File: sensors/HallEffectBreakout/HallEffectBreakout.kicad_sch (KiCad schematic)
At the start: 0 parts

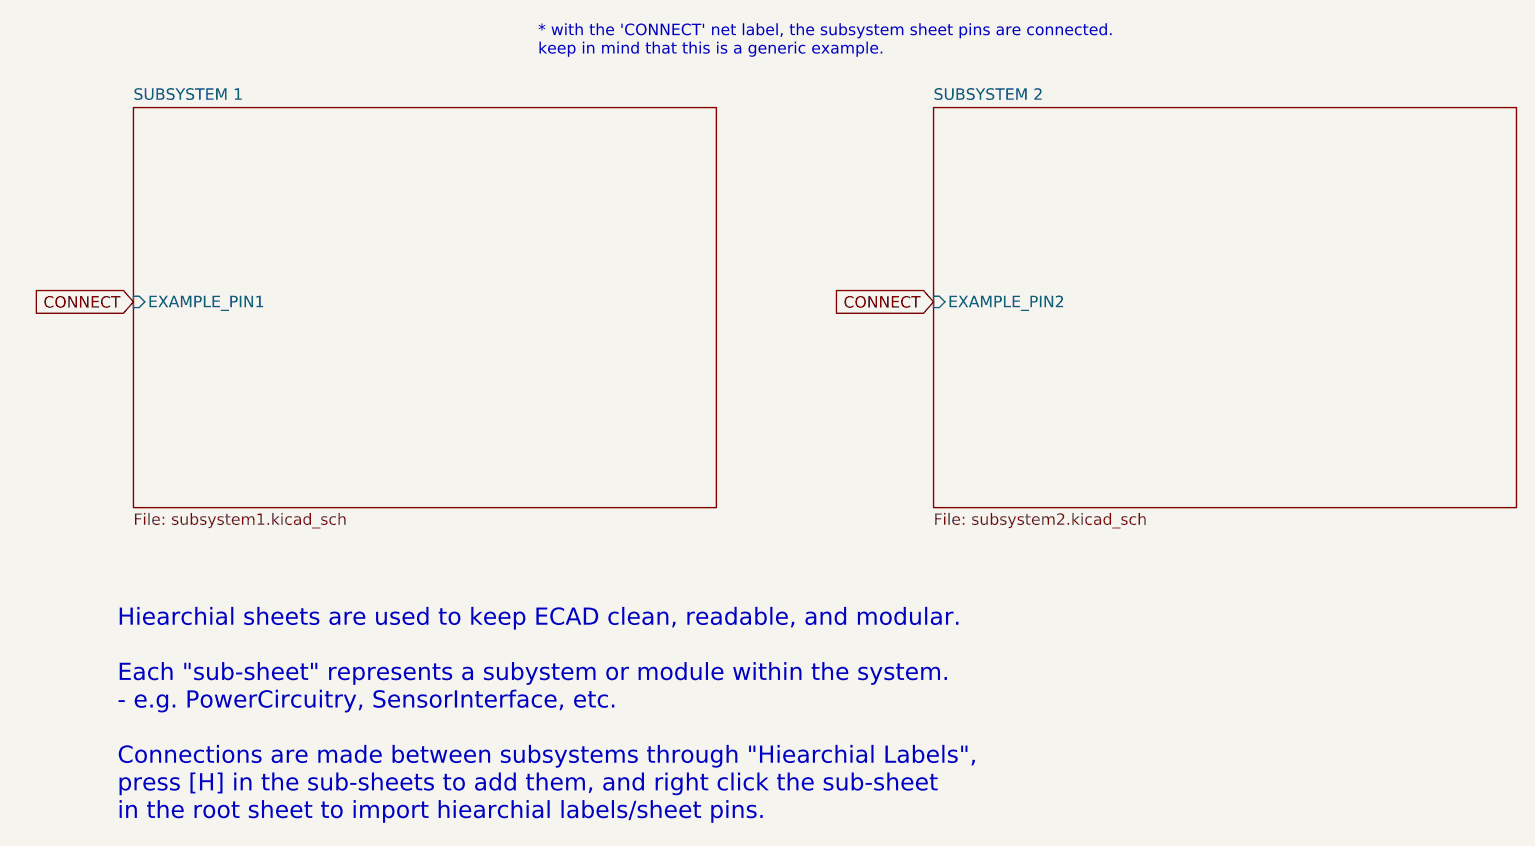
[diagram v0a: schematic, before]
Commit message: Removed Unused Template & Added TMAG5723
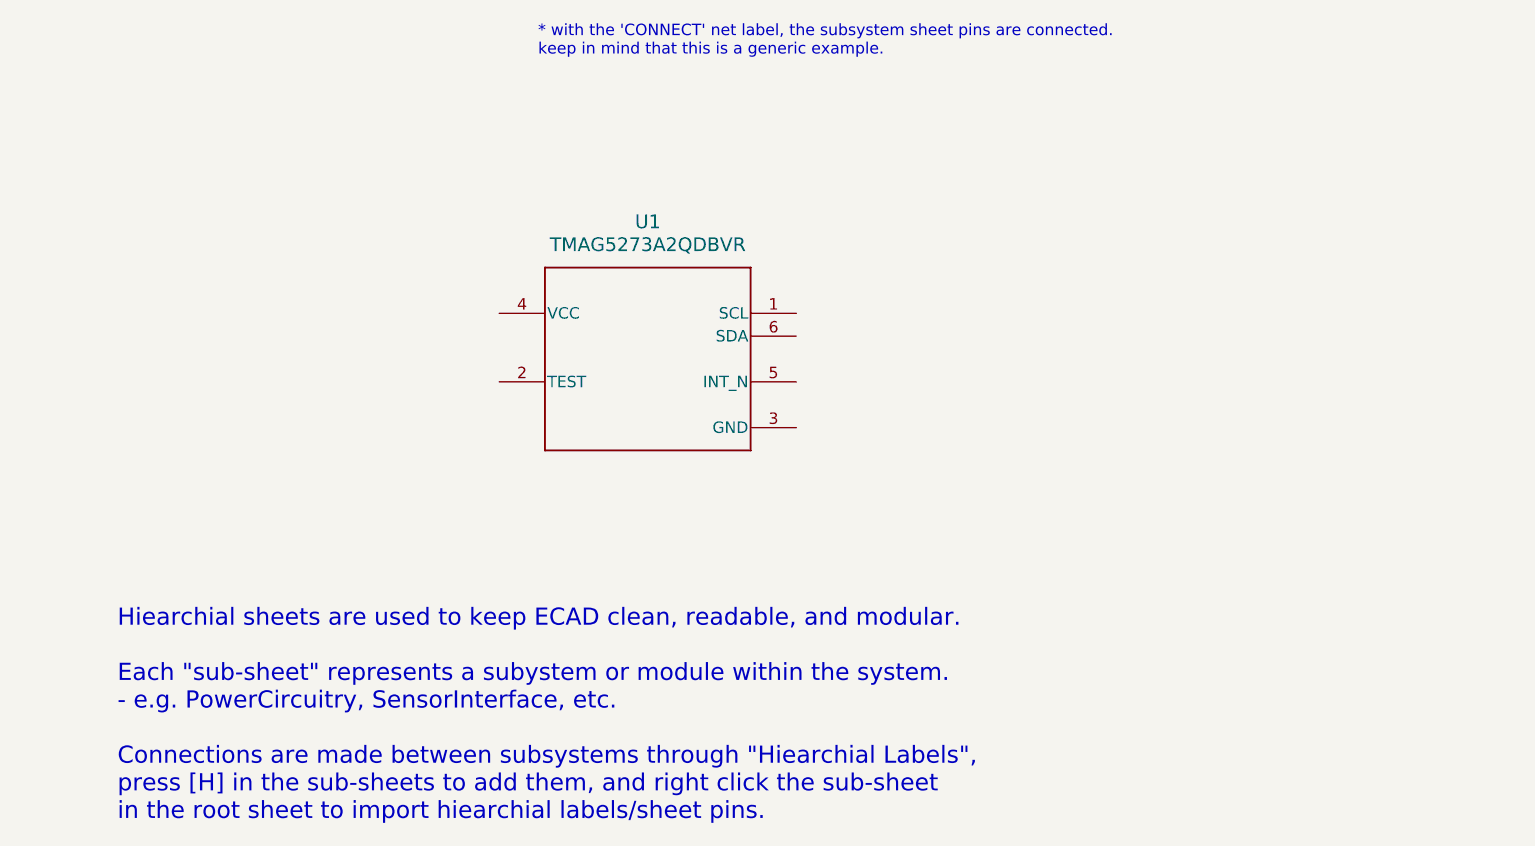
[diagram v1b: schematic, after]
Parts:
- added U1: TMAG5273A2QDBVR, DBV0006A-IPC_A, symbol TMAG5273:TMAG5273A2QDBVR
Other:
- removed sheet SUBSYSTEM 1
- removed sheet SUBSYSTEM 2
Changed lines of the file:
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@@
 		)
 	)
-	(global_label "CONNECT"
-		(shape input)
-		(at 72.39 88.9 180)
+	(symbol
+		(lib_id "TMAG5273:TMAG5273A2QDBVR")
+		(at 113.03 90.17 0)
+		(unit 1)
+		(body_style 1)
+		(exclude_from_sim no)
+		(in_bom yes)
+		(on_board yes)
+		(in_pos_files yes)
+		(dnp no)
 		(fields_autoplaced yes)
-		(effects
-			(font
-				(size 1.27 1.27)
+		(property "Reference" "U1"
+			(at 129.54 80.01 0)
+			(show_name no)
+			(do_not_autoplace no)
+			(effects
+				(font
+					(size 1.524 1.524)
+				)
 			)
-			(justify right)
 		)
-		(property "Intersheetrefs" "${INTERSHEET_REFS}"
-			(at 60.7567 88.9 0)
+		(property "Value" "TMAG5273A2QDBVR"
+			(at 129.54 82.55 0)
+			(show_name no)
+			(do_not_autoplace no)
+			(effects
+				(font
+					(size 1.524 1.524)
+				)
+			)
+		)
+		(property "Footprint" "DBV0006A-IPC_A"
+			(at 113.03 90.17 0)
+			(hide yes)
+			(show_name no)
+			(do_not_autoplace no)
+			(effects
+				(font
+					(size 1.27 1.27)
+					(italic yes)
+				)
+			)
+		)
+		(property "Datasheet" "https://www.ti.com/lit/gpn/tmag5273"
+			(at 113.03 90.17 0)
+			(hide yes)
+			(show_name no)
+			(do_not_autoplace no)
+			(effects
+				(font
+					(size 1.27 1.27)
+					(italic yes)
+				)
+			)
+		)
+		(property "Description" ""
+			(at 113.03 90.17 0)
 			(hide yes)
 			(show_name no)
@@
 					(size 1.27 1.27)
 				)
-				(justify right)
 			)
 		)
-	)
-	(global_label "CONNECT"
-		(shape input)
-		(at 161.29 88.9 180)
-		(fields_autoplaced yes)
-		(effects
-			(font
-				(size 1.27 1.27)
-			)
-			(justify right)
+		(pin "6"
 		)
-		(property "Intersheetrefs" "${INTERSHEET_REFS}"
-			(at 149.6567 88.9 0)
-			(hide yes)
-			(show_name no)
-			(do_not_autoplace no)
-			(effects
-				(font
-					(size 1.27 1.27)
-				)
-				(justify right)
-			)
+		(pin "4"
 		)
-	)
-	(sheet
-		(at 72.39 67.31)
-		(size 64.77 44.45)
-		(exclude_from_sim no)
-		(in_bom yes)
-		(on_board yes)
-		(dnp no)
-		(fields_autoplaced yes)
-		(stroke
-			(width 0.1524)
-			(type solid)
+		(pin "3"
 		)
-		(fill
-			(color 0 0 0 0)
+		(pin "5"
 		)
-		(property "Sheetname" "SUBSYSTEM 1"
-			(at 72.39 66.5984 0)
-			(show_name no)
-			(do_not_autoplace no)
-			(effects
-				(font
-					(size 1.27 1.27)
-				)
-				(justify left bottom)
-			)
+		(pin "2"
 		)
-		(property "Sheetfile" "subsystem1.kicad_sch"
-			(at 72.39 112.3446 0)
-			(show_name no)
-			(do_not_autoplace no)
-			(effects
-				(font
-					(size 1.27 1.27)
-				)
-				(justify left top)
-			)
-		)
-		(pin "EXAMPLE_PIN1" input
-			(at 72.39 88.9 180)
-			(effects
-				(font
-					(size 1.27 1.27)
-				)
-				(justify left)
-			)
+		(pin "1"
 		)
 		(instances
 			(project "HallEffectBreakout"
 				(path "/5d0263c1-1fe6-4a09-9aab-0edd61f61b2d"
-					(page "2")
+					(reference "U1")
+					(unit 1)
 				)
 			)
-		)
-	)
-	(sheet
-		(at 161.29 67.31)
-		(size 64.77 44.45)
-		(exclude_from_sim no)
-		(in_bom yes)
-		(on_board yes)
-		(dnp no)
-		(fields_autoplaced yes)
-		(stroke
-			(width 0.1524)
-			(type solid)
-		)
-		(fill
-			(color 0 0 0 0)
-		)
-		(property "Sheetname" "SUBSYSTEM 2"
-			(at 161.29 66.5984 0)
-			(show_name no)
-			(do_not_autoplace no)
-			(effects
-				(font
-					(size 1.27 1.27)
-				)
-				(justify left bottom)
-			)
-		)
-		(property "Sheetfile" "subsystem2.kicad_sch"
-			(at 161.29 112.3446 0)
-			(show_name no)
-			(do_not_autoplace no)
-			(effects
-				(font
-					(size 1.27 1.27)
-				)
-				(justify left top)
-			)
-		)
-		(pin "EXAMPLE_PIN2" input
-			(at 161.29 88.9 180)
-			(effects
-				(font
-					(size 1.27 1.27)
-				)
-				(justify left)
-			)
-		)
-		(instances
-			(project "HallEffectBreakout"
-				(path "/5d0263c1-1fe6-4a09-9aab-0edd61f61b2d"
-					(page "3")
-				)
-			)
